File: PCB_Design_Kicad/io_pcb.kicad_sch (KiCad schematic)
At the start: 17 parts, among them J11 Conn_01x07, J12 Conn_01x07, J13 Conn_01x07, J17 MIDI in, J3 Voct_A, J4 Trig_A, J5 Vel_A, J6 Voct_B, J7 Trig_B, J8 Vel_B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

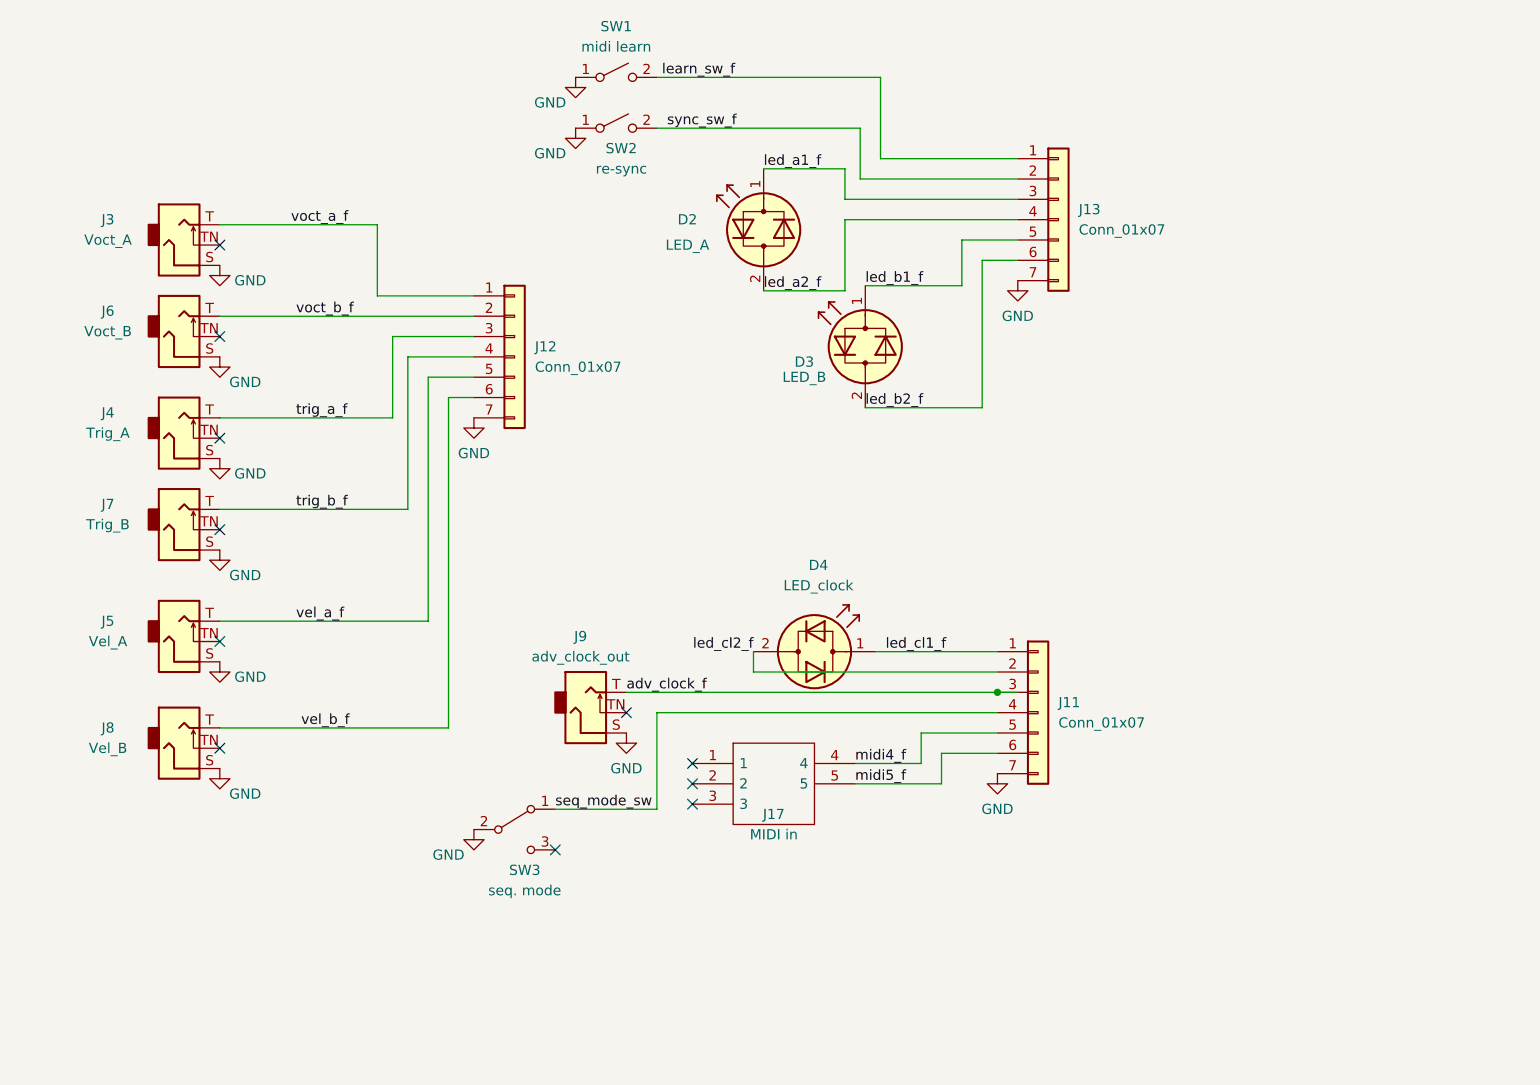
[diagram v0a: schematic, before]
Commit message: SMD pcb, routable and with vias
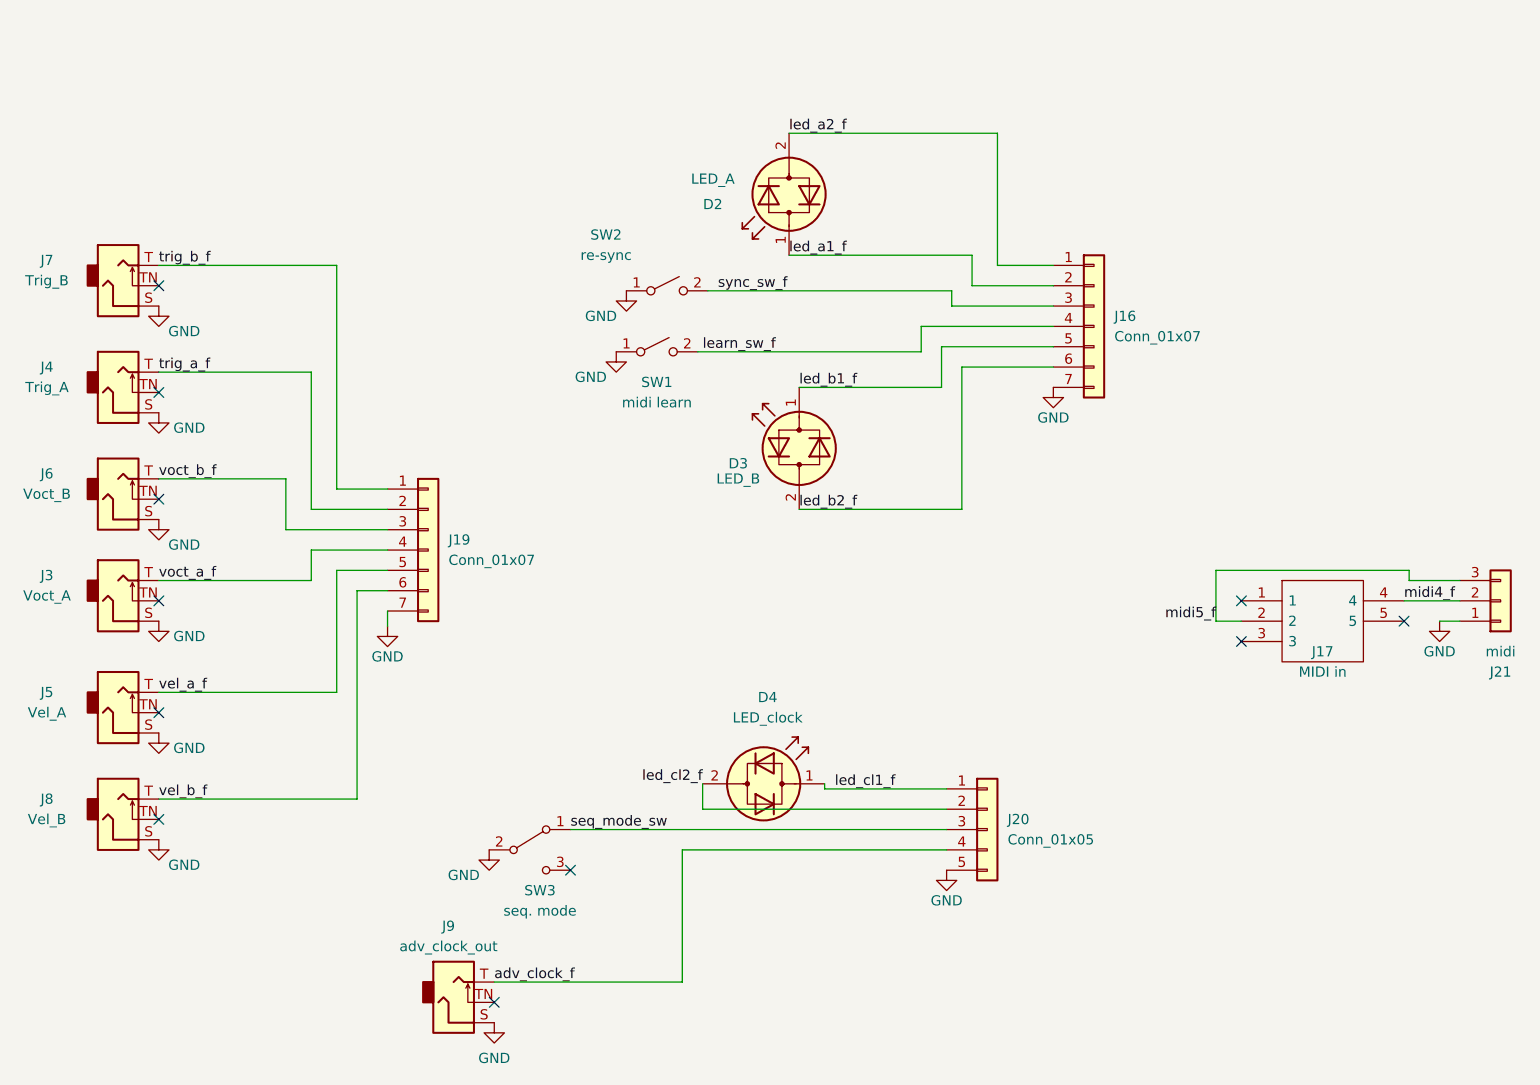
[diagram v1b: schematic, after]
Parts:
- removed J11, J12, J13: Conn_01x07, Connector_PinHeader_2.54mm:PinHeader_1x07_P2.54mm_Vertical, symbol Connector_Generic:Conn_01x07
- added J16, J19: Conn_01x07, Connector_PinHeader_2.54mm:PinHeader_1x07_P2.54mm_Vertical, symbol Connector_Generic:Conn_01x07
- added J20: Conn_01x05, Connector_PinHeader_2.54mm:PinHeader_1x05_P2.54mm_Vertical, symbol Connector_Generic:Conn_01x05
- added J21: midi, Connector_PinHeader_2.54mm:PinHeader_1x03_P2.54mm_Vertical, symbol Connector_Generic:Conn_01x03
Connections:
- net GND: now also J16.7 (Pin_7), J19.7 (Pin_7), J20.5 (Pin_5), J21.1 (Pin_1)
- net adv_clock_f: now also J20.4 (Pin_4)
- net learn_sw_f: now also J16.4 (Pin_4)
- net led_a1_f: now also J16.2 (Pin_2)
- net led_a2_f: now also J16.1 (Pin_1)
- net led_b1_f: now also J16.5 (Pin_5)
- net led_b2_f: now also J16.6 (Pin_6)
- net led_cl1_f: now also J20.1 (Pin_1)
- net led_cl2_f: now also J20.2 (Pin_2)
- net midi4_f: now also J21.2 (Pin_2)
- net midi5_f: now also J17.2, J21.3 (Pin_3); no longer J17.5
- net seq_mode_sw: now also J20.3 (Pin_3)
- net sync_sw_f: now also J16.3 (Pin_3)
- net trig_a_f: now also J19.2 (Pin_2)
- net trig_b_f: now also J19.1 (Pin_1)
- net vel_a_f: now also J19.5 (Pin_5)
- net vel_b_f: now also J19.6 (Pin_6)
- net voct_a_f: now also J19.4 (Pin_4)
- net voct_b_f: now also J19.3 (Pin_3)
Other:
- moved on the sheet: D2, D3, D4, J17, J3, J4, J5, J6, J7, J8, J9, SW1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

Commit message: routed SMD
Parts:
- removed J16, J19: Conn_01x07, Connector_PinHeader_2.54mm:PinHeader_1x07_P2.54mm_Vertical, symbol Connector_Generic:Conn_01x07
- removed J20: Conn_01x05, Connector_PinHeader_2.54mm:PinHeader_1x05_P2.54mm_Vertical, symbol Connector_Generic:Conn_01x05
- removed J21: midi, Connector_PinHeader_2.54mm:PinHeader_1x03_P2.54mm_Vertical, symbol Connector_Generic:Conn_01x03

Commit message: better routing
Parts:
- removed J17: MIDI in, SamacSys_Parts:SD-50BV, symbol SamacSys_Parts:SD-50BV
- added J12: front bottom, Connector_PinSocket_2.54mm:PinSocket_1x11_P2.54mm_Vertical, symbol Connector_Generic:Conn_01x11
- added J14: front top, Connector_PinSocket_2.54mm:PinSocket_1x07_P2.54mm_Vertical, symbol Connector_Generic:Conn_01x07
- SW1: value midi learn -> re-sync
- SW2: value re-sync -> midi learn
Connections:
- net GND: now also J12.11 (Pin_11), J14.7 (Pin_7)
- net adv_clock_f: now also J14.4 (Pin_4)
- net learn_sw_f: now also SW2.2 (B), J12.5 (Pin_5); no longer SW1.2 (B)
- net led_a1_f: now also J12.7 (Pin_7)
- net led_a2_f: now also J12.8 (Pin_8)
- net led_b1_f: now also J12.4 (Pin_4)
- net led_b2_f: now also J12.3 (Pin_3)
- net led_cl1_f: now also J12.10 (Pin_10)
- net led_cl2_f: now also J12.9 (Pin_9)
- net seq_mode_sw: now also J14.3 (Pin_3)
- net sync_sw_f: now also SW1.2 (B), J12.6 (Pin_6); no longer SW2.2 (B)
- net trig_a_f: now also J12.2 (Pin_2)
- net trig_b_f: now also J12.1 (Pin_1)
- net vel_a_f: now also J14.2 (Pin_2)
- net vel_b_f: now also J14.1 (Pin_1)
- net voct_a_f: now also J14.5 (Pin_5)
- net voct_b_f: now also J14.6 (Pin_6)
- no-connect marks 11 -> 8
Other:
- moved on the sheet: D2, D4, J3, J4, J5, J6, J7, J8

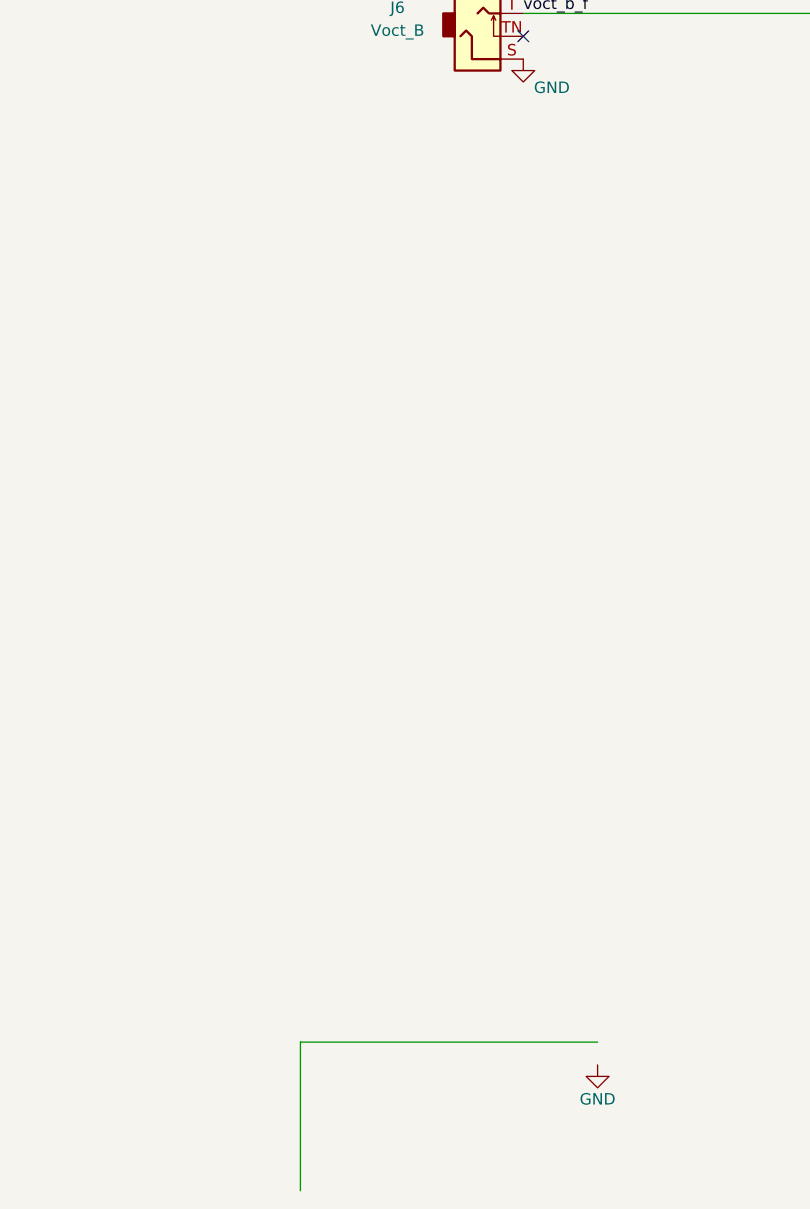
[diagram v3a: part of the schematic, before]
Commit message: adding to BOM
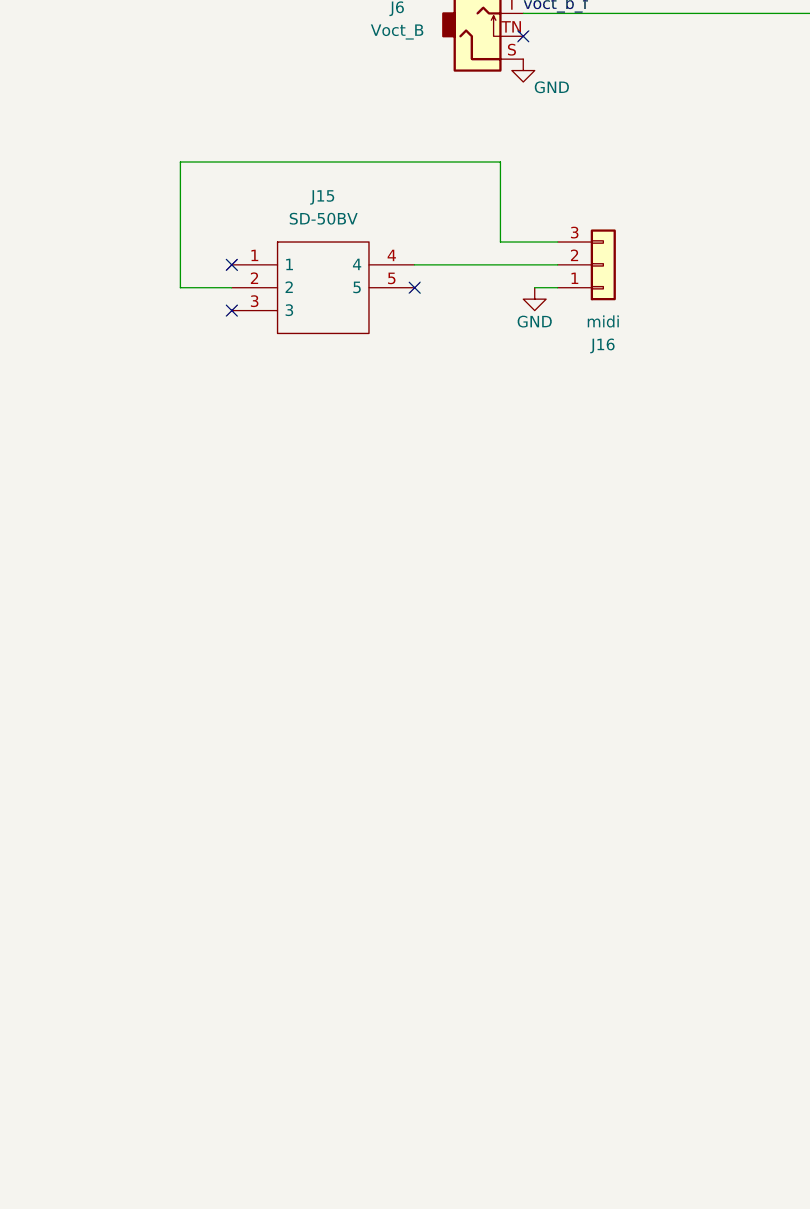
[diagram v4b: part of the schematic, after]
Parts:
- added J15: SD-50BV, SamacSys_Parts:SD-50BV, symbol SamacSys_Parts:SD-50BV
- added J16: midi, Connector_PinSocket_2.54mm:PinSocket_1x03_P2.54mm_Vertical, symbol Connector_Generic:Conn_01x03
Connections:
- net GND: now also J16.1 (Pin_1)
- new net: J15.2, J16.3 (Pin_3)
- new net: J15.4, J16.2 (Pin_2)
- no-connect marks 8 -> 11

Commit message: more bom
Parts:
- J15: footprint SamacSys_Parts:SD-50BV -> WeirdVibes_Eurorack:CUI SD-50BV MIDI DIN-5
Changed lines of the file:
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@@
+			)
+		)
+		(property "Comment" ""
+			(at 39.37 67.945 0)
+			(effects
+				(font
+					(size 1.27 1.27)
+				)
+				(hide yes)
 			)
 		)
@@
 			)
 		)
+		(property "Comment" ""
+			(at 152.4 75.565 0)
+			(effects
+				(font
+					(size 1.27 1.27)
+				)
+				(hide yes)
+			)
+		)
 		(pin "S"
 		)
@@
 			)
 		)
+		(property "Comment" ""
+			(at 53.975 55.245 0)
+			(effects
+				(font
+					(size 1.27 1.27)
+				)
+				(hide yes)
+			)
+		)
 		(pin "2"
 		)
@@
 			)
 		)
+		(property "Comment" ""
+			(at 152.4 38.1 0)
+			(effects
+				(font
+					(size 1.27 1.27)
+				)
+				(hide yes)
+			)
+		)
 		(pin "S"
 		)
@@
 			)
 		)
-		(property "Footprint" "SamacSys_Parts:SD-50BV"
+		(property "Footprint" "WeirdVibes_Eurorack:CUI SD-50BV MIDI DIN-5"
 			(at 141.605 133.985 0)
 			(effects
@@
 		)
 		(property "Price (single)" ""
+			(at 125.095 136.525 0)
+			(effects
+				(font
+					(size 1.27 1.27)
+				)
+				(hide yes)
+			)
+		)
+		(property "Comment" ""
 			(at 125.095 136.525 0)
 			(effects
@@
 			)
 		)
+		(property "Comment" ""
+			(at 152.4 23.495 0)
+			(effects
+				(font
+					(size 1.27 1.27)
+				)
+				(hide yes)
+			)
+		)
 		(pin "S"
 		)
@@
 		)
 		(property "Price (single)" ""
+			(at 36.83 76.2 0)
+			(effects
+				(font
+					(size 1.27 1.27)
+				)
+				(hide yes)
+			)
+		)
+		(property "Comment" ""
 			(at 36.83 76.2 0)
 			(effects
@@
 			)
 		)
+		(property "Comment" ""
+			(at 152.4 92.71 0)
+			(effects
+				(font
+					(size 1.27 1.27)
+				)
+				(hide yes)
+			)
+		)
 		(pin "S"
 		)
@@
 			)
 		)
+		(property "Comment" ""
+			(at 206.375 64.135 0)
+			(effects
+				(font
+					(size 1.27 1.27)
+				)
+				(hide yes)
+			)
+		)
 		(pin "2"
 		)
@@
 			)
 		)
+		(property "Comment" ""
+			(at 57.15 34.29 0)
+			(effects
+				(font
+					(size 1.27 1.27)
+				)
+				(hide yes)
+			)
+		)
 		(pin "S"
 		)
@@
 		)
 		(property "Price (single)" ""
+			(at 149.225 54.61 0)
+			(effects
+				(font
+					(size 1.27 1.27)
+				)
+				(hide yes)
+			)
+		)
+		(property "Comment" ""
 			(at 149.225 54.61 0)
 			(effects
@@
 			)
 		)
+		(property "Comment" ""
+			(at 152.4 108.585 0)
+			(effects
+				(font
+					(size 1.27 1.27)
+				)
+				(hide yes)
+			)
+		)
 		(pin "S"
 		)
@@
 			)
 		)
+		(property "Comment" ""
+			(at 166.37 136.525 0)
+			(effects
+				(font
+					(size 1.27 1.27)
+				)
+				(hide yes)
+			)
+		)
 		(pin "3"
 		)
@@
 			)
 		)
+		(property "Comment" ""
+			(at 51.435 113.03 0)
+			(effects
+				(font
+					(size 1.27 1.27)
+				)
+				(hide yes)
+			)
+		)
 		(pin "2"
 		)
@@
 		)
 		(property "Price (single)" ""
+			(at 57.785 90.805 0)
+			(effects
+				(font
+					(size 1.27 1.27)
+				)
+				(hide yes)
+			)
+		)
+		(property "Comment" ""
 			(at 57.785 90.805 0)
 			(effects
@@
 			)
 		)
+		(property "Comment" ""
+			(at 57.15 20.955 0)
+			(effects
+				(font
+					(size 1.27 1.27)
+				)
+				(hide yes)
+			)
+		)
 		(pin "S"
 		)
@@
 			(at 102.87 80.01 0)
 			(effects
+				(font
+					(size 1.27 1.27)
+				)
+				(hide yes)
+			)
+		)
+		(property "Comment" ""
+			(at 102.87 80.01 0)
+			(effects

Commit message: pcb
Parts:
- removed J15: SD-50BV, WeirdVibes_Eurorack:CUI SD-50BV MIDI DIN-5, symbol SamacSys_Parts:SD-50BV
- removed J16: midi, Connector_PinSocket_2.54mm:PinSocket_1x03_P2.54mm_Vertical, symbol Connector_Generic:Conn_01x03
- added IC2: DAC8562SDGSR, SamacSys_Parts:SOP50P490X110-10N, symbol SamacSys_Parts:DAC8562SDGSR
- added J15, J16: Conn_01x05, Connector_PinHeader_2.54mm:PinHeader_1x05_P2.54mm_Vertical, symbol Connector_Generic:Conn_01x05
- added J19, J22: bbjack, WeirdVibes:Thonkiconn, symbol WeirdVibes_Eurorack:AudioJack_Switch
- added J20, J21, J23, J24: Conn_01x03, Connector_PinHeader_2.54mm:PinHeader_1x03_P2.54mm_Vertical, symbol Connector_Generic:Conn_01x03
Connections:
- new net: J19.S, J20.3 (Pin_3), J21.3 (Pin_3)
- new net: J19.T, J20.1 (Pin_1), J21.1 (Pin_1)
- new net: J19.TN, J20.2 (Pin_2), J21.2 (Pin_2)
- new net: IC2.1 (VOUTA), J15.1 (Pin_1)
- new net: IC2.10 (VREFIN/VREFOUT), J16.1 (Pin_1)
- new net: IC2.2 (VOUTB), J15.2 (Pin_2)
- new net: IC2.3 (GND), J15.3 (Pin_3)
- new net: IC2.4 (~{LDAC}), J15.4 (Pin_4)
- new net: IC2.5 (~{CLR}), J15.5 (Pin_5)
- new net: IC2.6 (~{SYNC}), J16.5 (Pin_5)
- new net: IC2.7 (SCLK), J16.4 (Pin_4)
- new net: IC2.8 (DIN), J16.3 (Pin_3)
- new net: IC2.9 (AVDD), J16.2 (Pin_2)
- new net: J22.T, J23.1 (Pin_1), J24.1 (Pin_1)
- new net: J22.TN, J23.2 (Pin_2), J24.2 (Pin_2)
- new net: J22.S, J23.3 (Pin_3), J24.3 (Pin_3)
- no-connect marks 11 -> 8

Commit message: pcb versions sent to jlcpcb
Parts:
- removed IC2: DAC8562SDGSR, SamacSys_Parts:SOP50P490X110-10N, symbol SamacSys_Parts:DAC8562SDGSR
- removed J15, J16: Conn_01x05, Connector_PinHeader_2.54mm:PinHeader_1x05_P2.54mm_Vertical, symbol Connector_Generic:Conn_01x05
- removed J19, J22: bbjack, WeirdVibes:Thonkiconn, symbol WeirdVibes_Eurorack:AudioJack_Switch
- removed J20, J21, J23, J24: Conn_01x03, Connector_PinHeader_2.54mm:PinHeader_1x03_P2.54mm_Vertical, symbol Connector_Generic:Conn_01x03
